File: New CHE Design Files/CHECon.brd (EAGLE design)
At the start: 81.7 x 51.7 mm, 34 parts, among them U2 MAX232SOIC16, U3 RS485SOIC

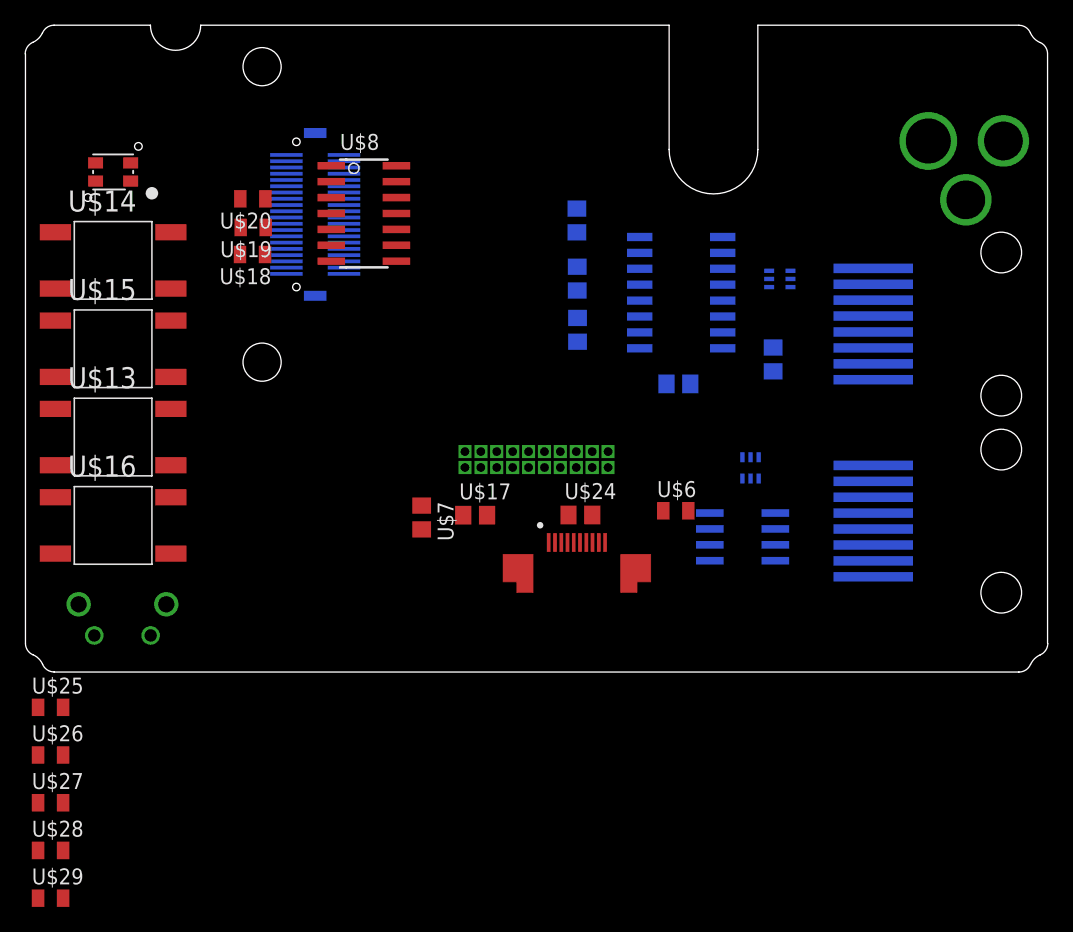
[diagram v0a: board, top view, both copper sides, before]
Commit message: P1
P1, seems to have errors
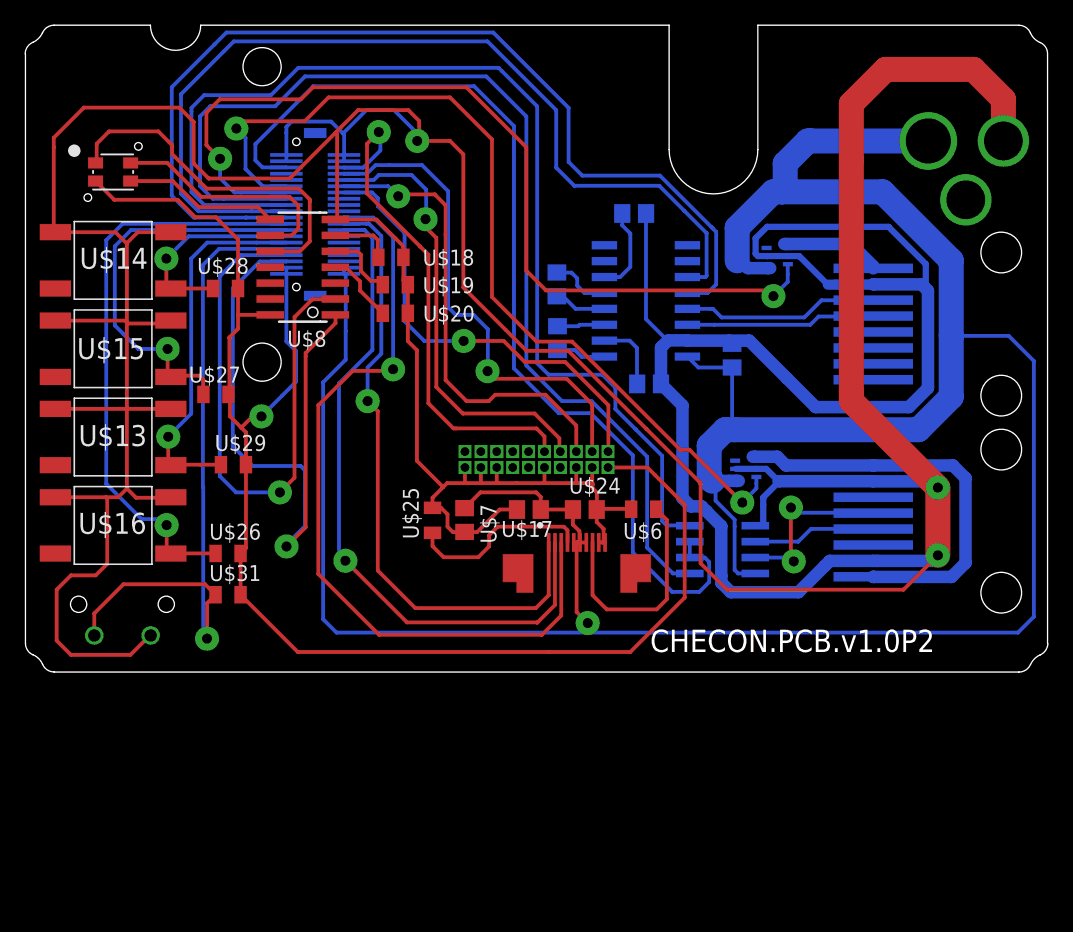
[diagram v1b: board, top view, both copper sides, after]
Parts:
- added U$31: (no value), GW-devices:RF-C0805
- U$30: value (none) -> RA_BUTTON
- moved U$28 47.0 mm to (-24.8, 4.80)
- moved U$29 37.6 mm to (-24.2, -9.27)
- moved U$27 35.2 mm to (-25.6, -3.66)
- moved U$25 34.0 mm to (-8.31, -13.7), turned to 90 degrees
- moved U$26 21.5 mm to (-24.6, -16.4)
- moved U$20 14.6 mm to (-11.3, 2.82), turned to 0 degrees
- moved U$19 12.2 mm to (-11.3, 5.11), turned to 0 degrees
- moved U$18 11.1 mm to (-11.6, 7.29), turned to 0 degrees
- moved U$8 6.50 mm to (-18.7, 6.50), turned to 90 degrees
- moved U$23 4.61 mm to (7.80, 10.8), turned to 180 degrees
- moved U$17 4.32 mm to (-0.61, -12.9), turned to 180 degrees
- moved U$7 3.44 mm to (-5.74, -13.7)
- moved U$21 3.29 mm to (15.6, -0.56)
- moved U2 2.90 mm to (8.74, 3.81)
- moved U$6 2.57 mm to (8.56, -12.8), turned to 180 degrees
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- renumbered E$10 to U$30
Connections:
- net +3V3: now also U$31.2; no longer U$17.1, U$2.P$5, U$2.P$6, U$2.P$7, U$24.1, U$7.1
- net GND: now also U$3.P$15, U$3.P$17, U$3.P$19, U$3.P$3, U$3.P$5, U$3.P$9, U$30.P$1
- net N$24: no longer U3.8
- net N$34: no longer U$16.3
- net N$35: no longer U$15.3
- net N$36: no longer U$14.3
- net N$37: no longer U$13.3
- net N$7: now also U$10.P$31, U$30.P$2, U$31.1; no longer U$3.P$15, U$3.P$17, U$3.P$19, U$3.P$3, U$3.P$5, U$3.P$9
- net V+: now also U$17.1, U$2.P$5, U$2.P$6, U$2.P$7, U$24.1, U$7.1, U3.8
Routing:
- net GND: track 0.00 -> 482.0 mm, vias 0 -> 3
- net V+: track 0.00 -> 234.0 mm, vias 0 -> 1
- net +3V3: track 0.00 -> 114.7 mm, vias 0 -> 1
- net N$27: track 0.00 -> 87.2 mm
- net N$17: track 0.00 -> 85.7 mm
- net N$10: track 0.00 -> 80.0 mm
- net N$28: track 0.00 -> 79.7 mm
- net N$26: track 0.00 -> 74.7 mm
- net N$40: track 0.00 -> 73.8 mm, vias 0 -> 2
- net N$39: track 0.00 -> 72.1 mm, vias 0 -> 2
- net N$31: track 0.00 -> 63.7 mm, vias 0 -> 1
- net N$29: track 0.00 -> 54.0 mm, vias 0 -> 1
- net N$7: track 0.00 -> 53.7 mm, vias 0 -> 1
- net N$11: track 0.00 -> 51.1 mm, vias 0 -> 1
- net N$30: track 0.00 -> 50.4 mm, vias 0 -> 1
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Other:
- board text added: "CHECON.PCB.v1.0P2"

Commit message: P2
Fixed LED, reset switch, scanner RTS, flipped FPC
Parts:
- removed U$31: (no value), GW-devices:RF-C0805
- U$2: value 52745-1097 -> (none)
- moved U$25 16.7 mm to (8.36, -12.9), turned to 0 degrees
- moved U$6 9.25 mm to (-0.69, -12.9)
- moved U$17 5.69 mm to (-5.74, -15.3), turned to 0 degrees
- moved U$23 2.05 mm to (5.77, 11.0)
- moved U$7 0.99 mm to (-5.74, -12.7), turned to 0 degrees
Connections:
- new net N$41: U$10.P$25, U2.10
- net +3V3: no longer U$31.2
- net N$35: now also U$10.P$31; no longer U$10.P$25
- net N$6: now also U$30.P$2
- net N$7: now also SCANNER.P$6, U2.7; no longer U$10.P$31, U$30.P$2, U$31.1
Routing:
- net N$41: track 0.00 -> 81.5 mm, vias 0 -> 2
- net N$6: track 40.7 -> 115.0 mm, vias 1 -> 2
- net N$34: track 47.4 -> 76.2 mm
- net N$7: track 53.7 -> 35.8 mm, vias 1 -> 2
- net N$32: track 18.5 -> 3.90 mm
- net V+: track 234.0 -> 246.8 mm
- net N$35: track 31.9 -> 20.2 mm
- net N$30: track 50.4 -> 60.7 mm
- net N$31: track 63.7 -> 54.0 mm
- net N$33: track 14.8 -> 5.49 mm
- net GND: track 482.0 -> 473.8 mm
- net N$29: track 54.0 -> 57.2 mm
- net N$22: track 6.94 -> 9.66 mm
- net N$4: track 39.2 -> 40.3 mm
- net +3V3: track 114.7 -> 113.7 mm
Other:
- board text added: "P2: Fixed LED, reset switch, scanner RTS, flipped FPC pinout"

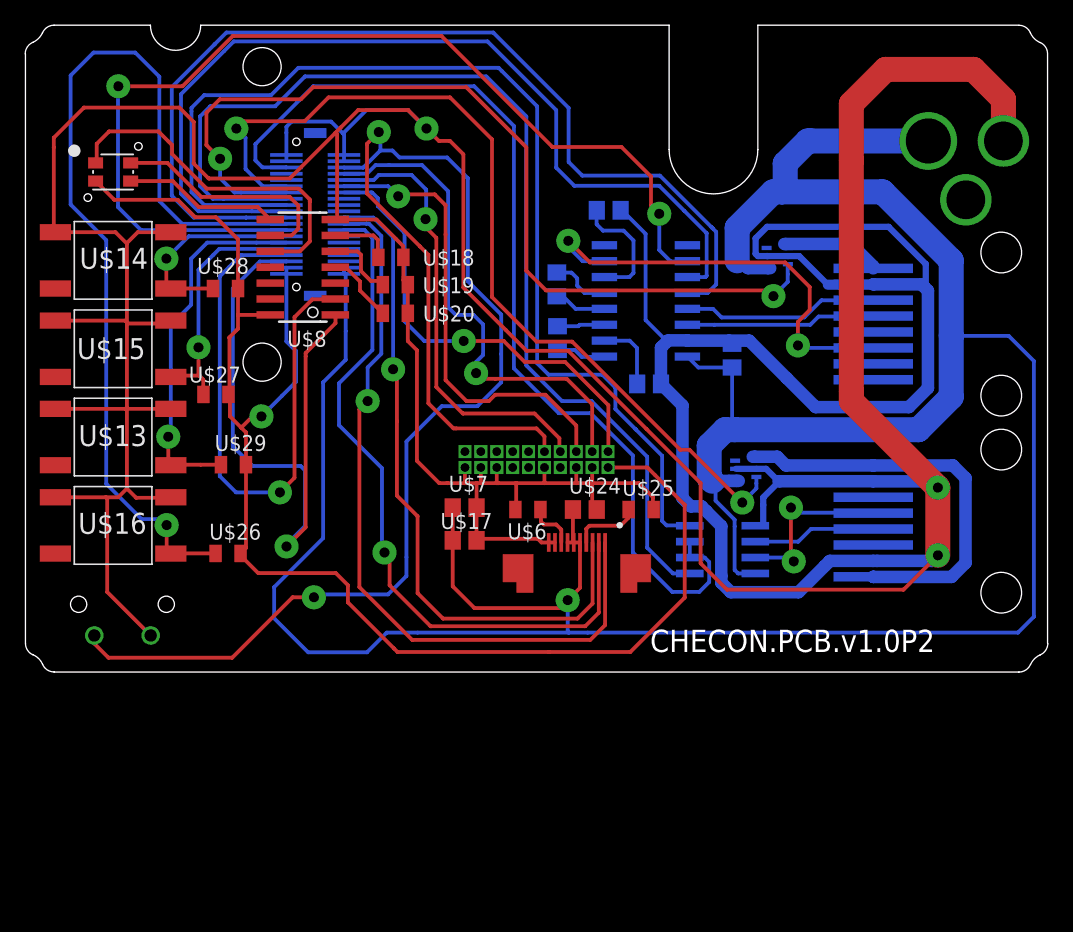
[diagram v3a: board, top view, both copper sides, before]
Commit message: P3 - in progress
Added 0.4mm spacing, need level shifter and other screen changes
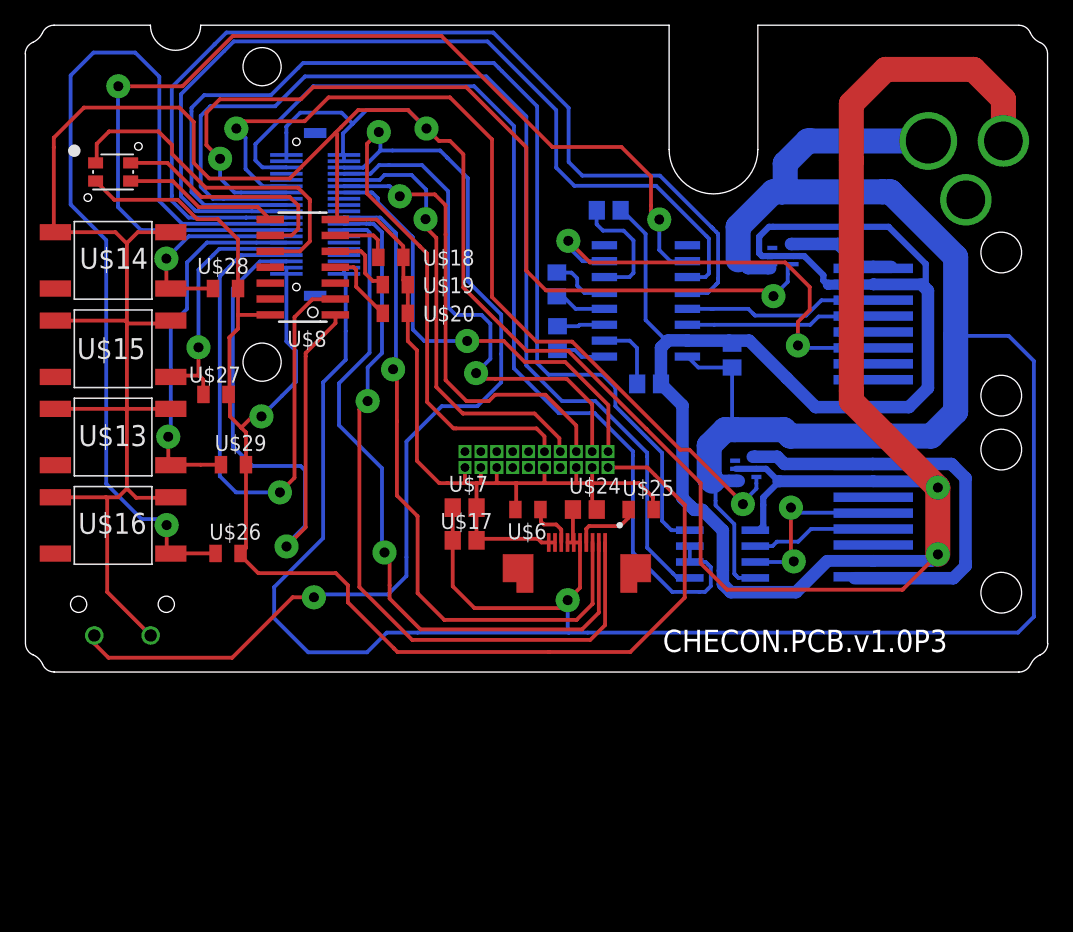
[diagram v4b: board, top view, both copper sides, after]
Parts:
- moved U$4 0.46 mm to (19.7, 7.39)
- moved U3 0.36 mm to (14.9, -16.4)
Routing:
- net N$24: track 32.7 -> 36.0 mm
- net V+: track 246.8 -> 249.6 mm
- net GND: track 473.8 -> 474.8 mm
- net N$4: track 40.3 -> 41.2 mm
- net N$25: track 8.41 -> 9.26 mm
- net N$29: track 57.2 -> 57.9 mm
- net N$31: track 54.0 -> 54.6 mm
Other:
- board text added: "CHECON.PCB.v1.0P3"
- board text added: "P3: Adjusted traces to use 0.4mm tool, need to add level shifter"
- board text removed: "CHECON.PCB.v1.0P2"
- board text removed: "P2: Fixed LED, reset switch, scanner RTS, flipped FPC pinout"
